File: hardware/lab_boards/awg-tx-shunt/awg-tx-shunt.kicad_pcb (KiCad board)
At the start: 2 copper layers, 66 x 57.1 mm, 12 parts, among them J1 FROM PWR AMP, J2 TX, J3 SHUNT

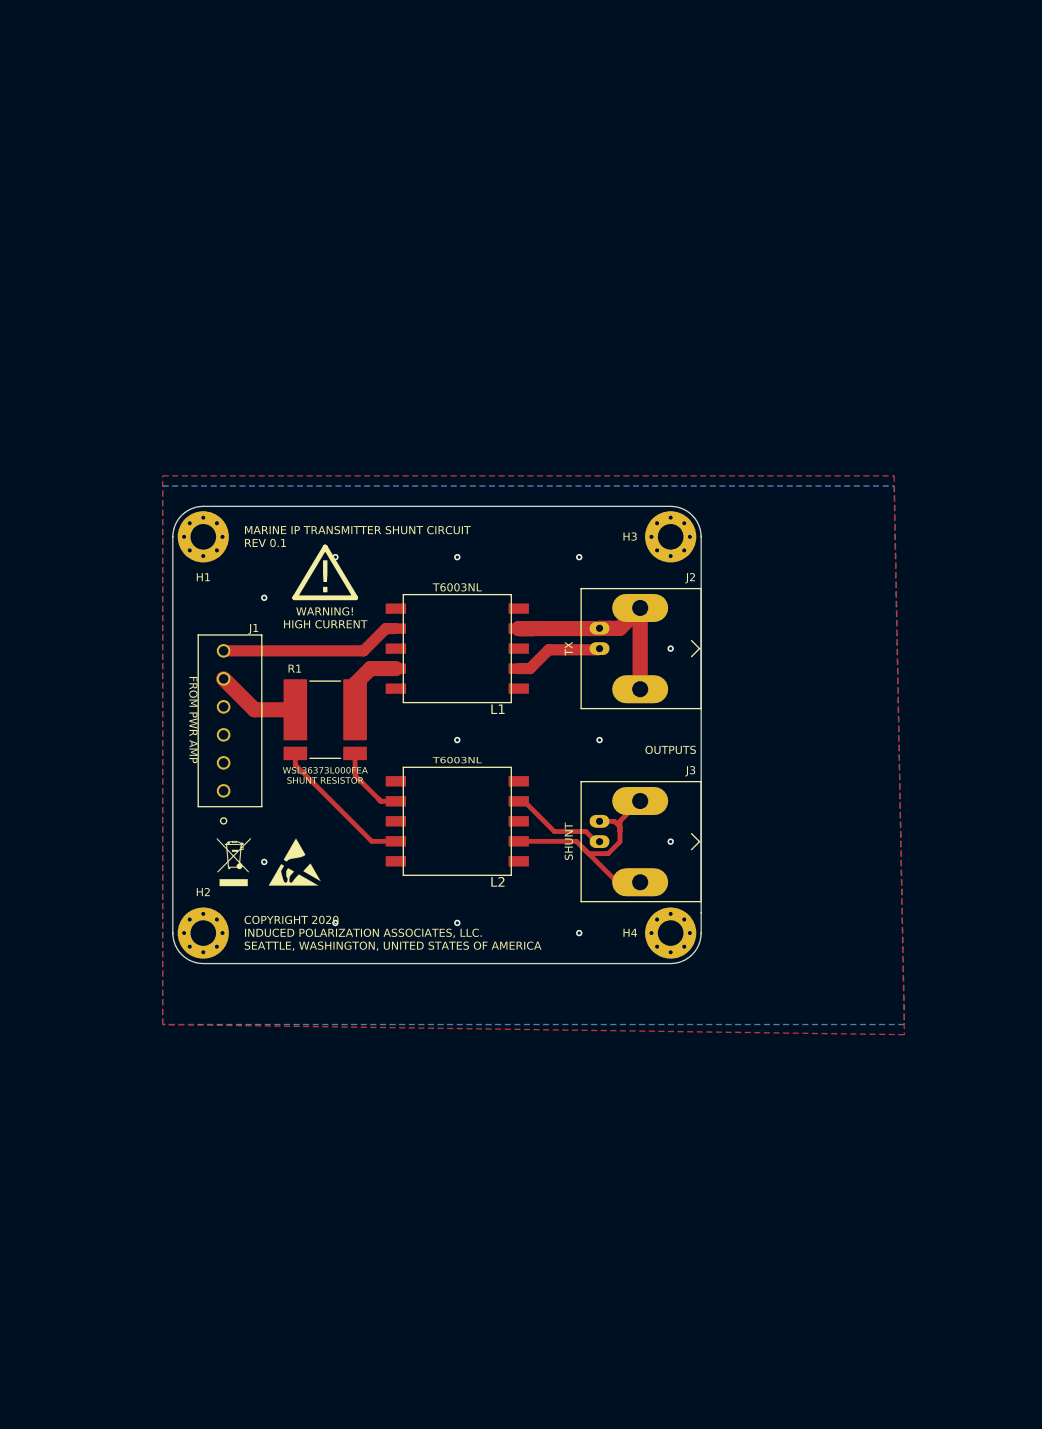
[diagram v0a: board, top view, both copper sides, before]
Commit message: Reworked the isolation and grounding scheme, added two shunt resistors and two connectors for each.
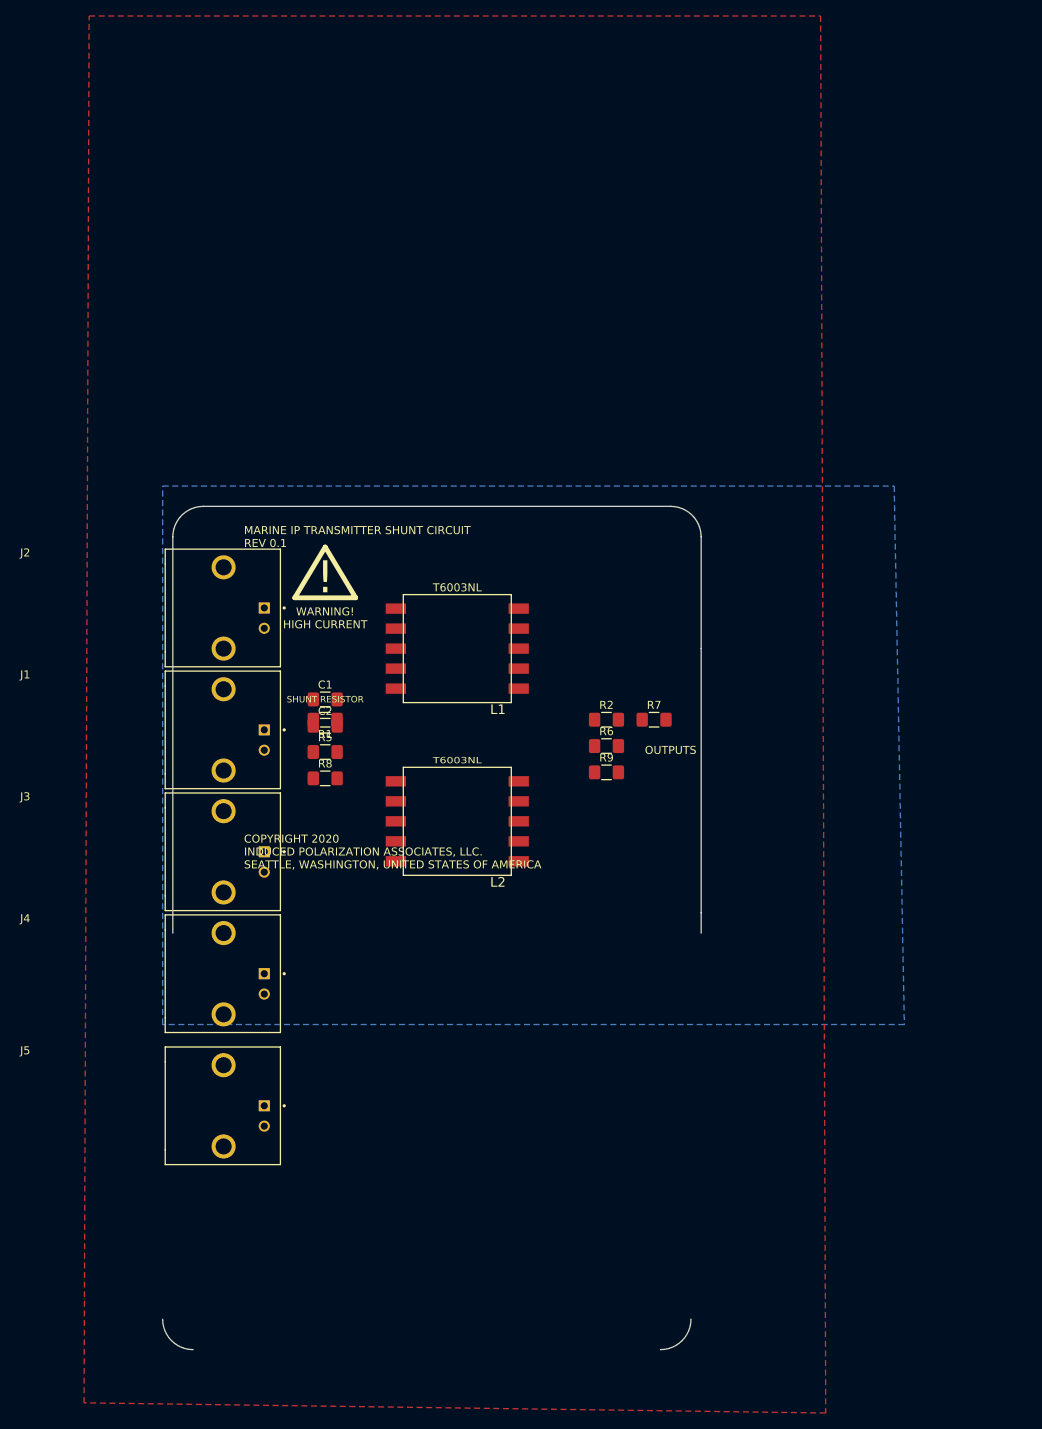
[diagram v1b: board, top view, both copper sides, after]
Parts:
- removed H1, H2, H3, H4: MountingHole, MountingHole:MountingHole_3.2mm_M3_Pad_Via
- removed REF**: ESD-Logo_6.6x6mm_SilkScreen, Symbol:ESD-Logo_6.6x6mm_SilkScreen
- removed REF**: WEEE-Logo_4.2x6mm_SilkScreen, Symbol:WEEE-Logo_4.2x6mm_SilkScreen
- added C1: 1uF C0G, Capacitor_SMD:C_1206_3216Metric_Pad1.42x1.75mm_HandSolder, F.Cu at (95.2, 100.3)
- added C2: 1uF C0G, Capacitor_SMD:C_1206_3216Metric_Pad1.42x1.75mm_HandSolder, F.Cu at (95.2, 103.6)
- added J4: 1-1337543-0, amphenol-isolated-pcb-mount-bnc:CONN_1-1337543-0, F.Cu at (87.6, 134.6)
- added J5: 1-1337543-0, amphenol-isolated-pcb-mount-bnc:CONN_1-1337543-0, F.Cu at (87.6, 151.1)
- added R2: 1M, Resistor_SMD:R_1206_3216Metric_Pad1.42x1.75mm_HandSolder, F.Cu at (130.4, 102.9)
- added R5: 1M, Resistor_SMD:R_1206_3216Metric_Pad1.42x1.75mm_HandSolder, F.Cu at (95.2, 106.9)
- added R6: 1M, Resistor_SMD:R_1206_3216Metric_Pad1.42x1.75mm_HandSolder, F.Cu at (130.4, 106.2)
- added R7: 70R, Resistor_SMD:R_1206_3216Metric_Pad1.42x1.75mm_HandSolder, F.Cu at (136.4, 102.9)
- added R8: 1M, Resistor_SMD:R_1206_3216Metric_Pad1.42x1.75mm_HandSolder, F.Cu at (95.2, 110.2)
- added R9: 70R, Resistor_SMD:R_1206_3216Metric_Pad1.42x1.75mm_HandSolder, F.Cu at (130.4, 109.5)
- J1: value FROM PWR AMP -> 1-1337543-0; footprint phoenix-6pos-1984659:1984659 -> amphenol-isolated-pcb-mount-bnc:CONN_1-1337543-0
- J2: value TX -> 1-1337543-0; footprint Connector_Coaxial:BNC_Amphenol_B6252HB-NPP3G-50_Horizontal -> amphenol-isolated-pcb-mount-bnc:CONN_1-1337543-0
- J3: value SHUNT -> 1-1337543-0; footprint Connector_Coaxial:BNC_Amphenol_B6252HB-NPP3G-50_Horizontal -> amphenol-isolated-pcb-mount-bnc:CONN_1-1337543-0
- R1: value WSL36373L000FEA -> 100K; footprint WSL36373L000FEA:WSL36373L000FEA -> Resistor_SMD:R_1206_3216Metric_Pad1.42x1.75mm_HandSolder
- moved J2 42.2 mm to (87.6, 88.9), turned to 0 degrees
- moved J3 41.9 mm to (87.6, 119.4), turned to 0 degrees
- moved J1 9.16 mm to (87.6, 104.1), turned to 0 degrees
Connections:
- J1 pad 1: GNDPWR -> /TX1_IN
- J1 pad 2: GNDPWR -> /TX2_IN
- J2 pad 1: Net-(J2-Pad1) -> (no net)
- J2 pad 2: Net-(J2-Pad2) -> (no net)
- J3 pad 1: Net-(J3-Pad1) -> (no net)
- J3 pad 2: Net-(J3-Pad2) -> (no net)
- L1 pad P$2: /TX1 -> /TX2_IN
- L1 pad P$4: Net-(L1-PadP$4) -> (no net)
- L1 pad P$7: Net-(J2-Pad1) -> /POWERAMP_IN_N
- L1 pad P$9: Net-(J2-Pad2) -> Net-(L1-PadP$9)
- L2 pad P$2: /SHUNT_N -> Net-(L2-PadP$2)
- L2 pad P$4: /SHUNT_P -> Net-(C2-Pad1)
- L2 pad P$7: Net-(J3-Pad2) -> Net-(J5-Pad2)
- L2 pad P$9: Net-(J3-Pad1) -> Net-(J5-Pad1)
- R1 pad 1: Net-(L1-PadP$4) -> Net-(C1-Pad2)
- R1 pad 2: /SHUNT_N -> /TX1_IN
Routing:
- net Net-(J3-Pad2): track 35.6 -> 0.00 mm
- net Net-(J2-Pad2): track 28.3 -> 0.00 mm
- net /TX1: track 22.7 -> 0.00 mm
- net /SHUNT_P: track 18.0 -> 0.00 mm
- net Net-(J3-Pad1): track 12.5 -> 0.00 mm
- net Net-(J2-Pad1): track 11.1 -> 0.00 mm
- net /TX2: track 10.6 -> 0.00 mm
- net /SHUNT_N: track 9.61 -> 0.00 mm
- net Net-(L1-PadP$4): track 9.11 -> 0.00 mm
- net GNDPWR: vias 12 -> 0
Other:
- board size 66 x 57.1 mm -> 67.3 x 105.4 mm

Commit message: reworked the whole board so the grounds are properly isolated and can be connected to a common star ground offboard. No vias are necessary for routing, either, which is a good thing for signal integrity.
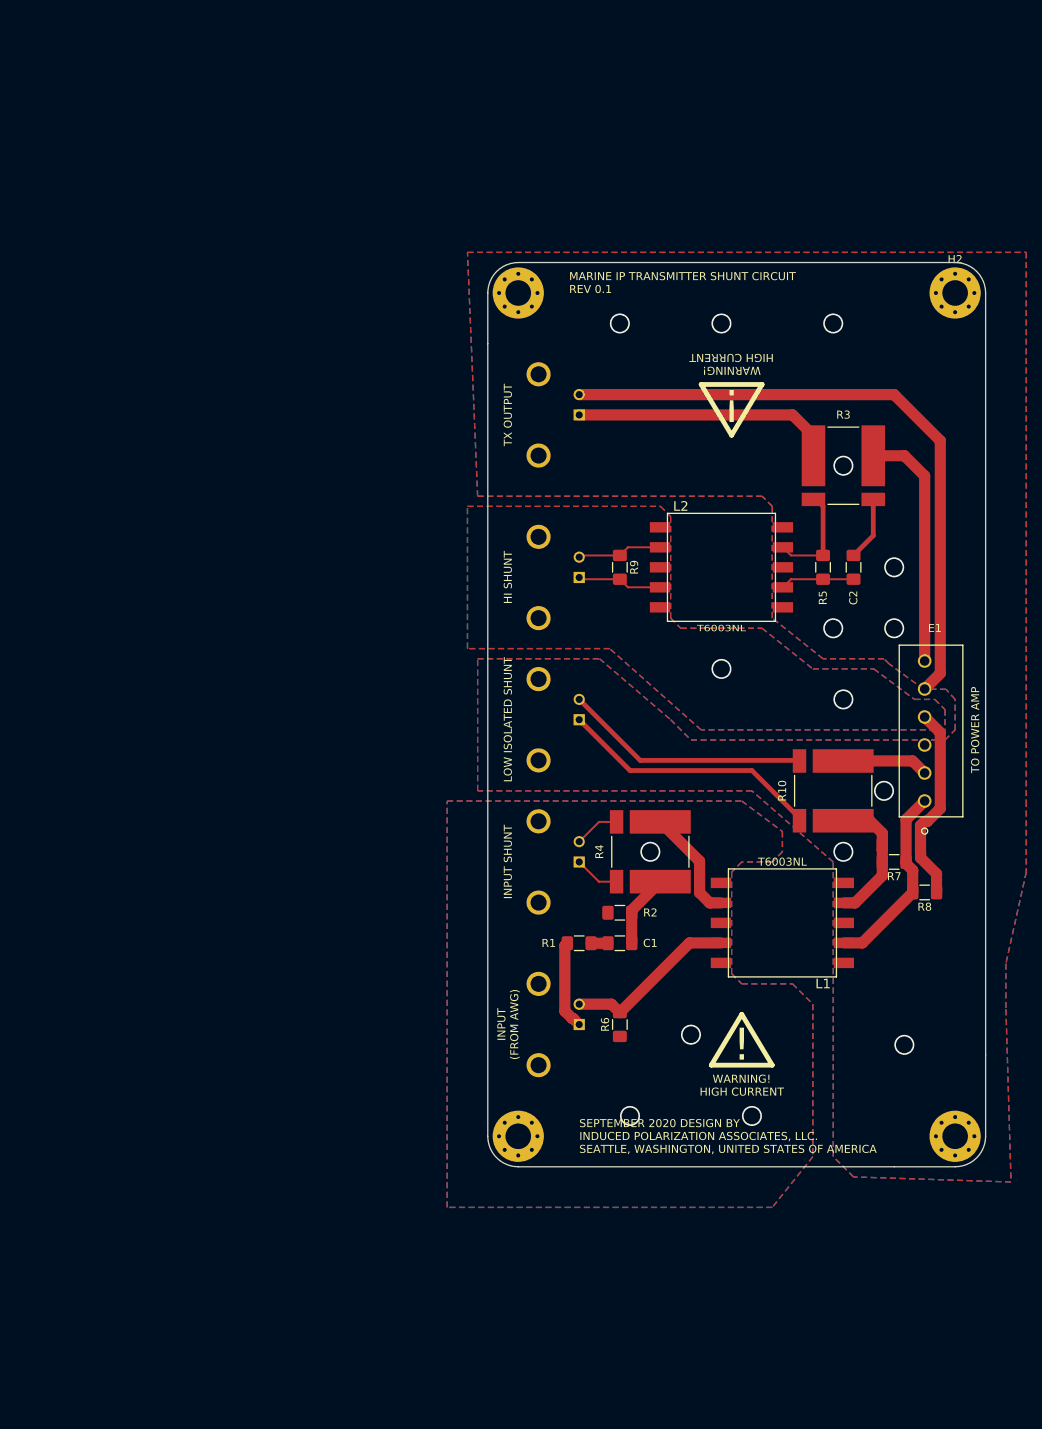
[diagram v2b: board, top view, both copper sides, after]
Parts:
- added E1: TO POWER AMP, phoenix-6pos-1984659:1984659, F.Cu at (170.2, 113.0)
- added H1: MountingHole, MountingHole:MountingHole_3.2mm_M3_Pad_Via, F.Cu at (119.4, 49.5)
- added H2: MountingHole, MountingHole:MountingHole_3.2mm_M3_Pad_Via, F.Cu at (174.0, 49.5)
- added H3: MountingHole, MountingHole:MountingHole_3.2mm_M3_Pad_Via, F.Cu at (119.4, 154.9)
- added H4: MountingHole, MountingHole:MountingHole_3.2mm_M3_Pad_Via, F.Cu at (174.0, 154.9)
- added R10: WSL36373L000FEA (3mOhm), WSL36373L000FEA:WSL36373L000FEA, F.Cu at (158.8, 111.8)
- added R3: WSL36373L000FEA (3mOhm), WSL36373L000FEA:WSL36373L000FEA, F.Cu at (160.0, 71.1)
- added R4: WSL36373L000FEA (3mOhm), WSL36373L000FEA:WSL36373L000FEA, F.Cu at (135.9, 119.4)
- J1, J2, J3, J4, J5: moved to B.Cu
- moved J4 80.2 mm to (127.0, 64.8)
- moved J5 76.9 mm to (127.0, 85.1)
- moved R8 76.3 mm to (170.2, 124.5), turned to 180 degrees
- moved C2 68.9 mm to (161.3, 83.8), turned to 90 degrees
- moved R5 66.4 mm to (157.5, 83.8), turned to 270 degrees
- moved J1 53.9 mm to (127.0, 141.0)
- moved L1 53.2 mm to (152.4, 128.3)
- moved J2 50.6 mm to (127.0, 120.7)
- moved C1 47.8 mm to (132.1, 130.8), turned to 180 degrees
- moved L2 45.8 mm to (144.8, 83.8), turned to 90 degrees
- moved J3 42.7 mm to (127.0, 102.9)
- moved R1 42.3 mm to (127.0, 130.8)
- moved R7 34.9 mm to (166.4, 120.7), turned to 180 degrees
- moved R6 34.9 mm to (132.1, 141.0), turned to 90 degrees
- moved R9 25.7 mm to (132.1, 83.8), turned to 270 degrees
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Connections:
- net Net-(J5-Pad1) renamed /HI_SHUNT_P
- net Net-(J5-Pad2) renamed /HI_SHUNT_N
- C2 pad 2: (no net) -> Net-(C2-Pad2)
- J2 pad 1: (no net) -> /INSHUNT_P
- J2 pad 2: (no net) -> /INSHUNT_N
- J3 pad 1: (no net) -> /LOW_SHUNT__ISO_P
- J3 pad 2: (no net) -> /LOW_SHUNT__ISO_N
- J4 pad 1: (no net) -> /TX1_OUT
- J4 pad 2: (no net) -> /TX2_OUT
- L1 pad P$2: /TX2_IN -> Net-(L1-PadP$2)
- L1 pad P$4: (no net) -> /TX2_IN
- L2 pad P$2: Net-(L2-PadP$2) -> Net-(C2-Pad1)
- L2 pad P$4: Net-(C2-Pad1) -> Net-(L2-PadP$4)
- R5 pad 1: Net-(L2-PadP$2) -> Net-(L2-PadP$4)
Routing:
- net /TX2_OUT: track 0.00 -> 79.4 mm
- net /LOW_SHUNT__ISO_P: track 0.00 -> 33.0 mm
- net /TX1_OUT: track 0.00 -> 32.9 mm
- net /LOW_SHUNT__ISO_N: track 0.00 -> 30.7 mm
- net /POWERAMP_OUT_P: track 0.00 -> 30.6 mm
- net GNDREF: track 0.00 -> 24.8 mm, vias 0 -> 2
- net /POWERAMP_IN_N: track 0.00 -> 24.0 mm
- net /TX2_IN: track 0.00 -> 21.8 mm
- net Net-(L1-PadP$9): track 0.00 -> 18.3 mm
- net Net-(L1-PadP$2): track 0.00 -> 14.1 mm
- net Net-(L2-PadP$4): track 0.00 -> 13.1 mm
- net /TX1_IN: track 0.00 -> 11.1 mm
- net /POWERAMP_IN_P: track 0.00 -> 10.8 mm
- net /HI_SHUNT_N: track 0.00 -> 10.6 mm
- net /HI_SHUNT_P: track 0.00 -> 10.6 mm
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- added copper zone on B.Cu, net GNDREF
- added copper zone on F.Cu, net GNDREF
- added copper zone on B.Cu, net GNDS
- added copper zone on F.Cu, net GNDS
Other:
- board size 67.3 x 105.4 mm -> 62.2 x 113 mm
- board text added: "HI SHUNT"
- board text added: "INPUT"
- board text added: "INPUT (FROM AWG)"
- board text added: "INPUT SHUNT"
- board text added: "LOW ISOLATED SHUNT"
- board text added: "SEPTEMBER 2020 DESIGN BY INDUCED POLARIZATION ASSOCIATES, LLC. SEATTLE, WASHINGTON, UNITED STATES OF AMERICA"
- board text added: "TX OUTPUT"
- board text removed: "COPYRIGHT 2020 INDUCED POLARIZATION ASSOCIATES, LLC. SEATTLE, WASHINGTON, UNITED STATES OF AMERICA"
- board text removed: "OUTPUTS"
- board text removed: "SHUNT RESISTOR"
